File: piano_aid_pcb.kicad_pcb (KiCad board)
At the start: 2 copper layers, 44.4 x 61 mm, 35 parts, among them J1 Barrel_Jack_MountingPin, J2 796644-3, J3 DIN-5_180degree, J4 Conn_01x06_Female, J5 Micro_SD_Card_Det, J6 Conn_01x07_Female, U1 317030213, U2 6N138, U3 74AHCT1G125W5-7, U4 AZ1117-3.3

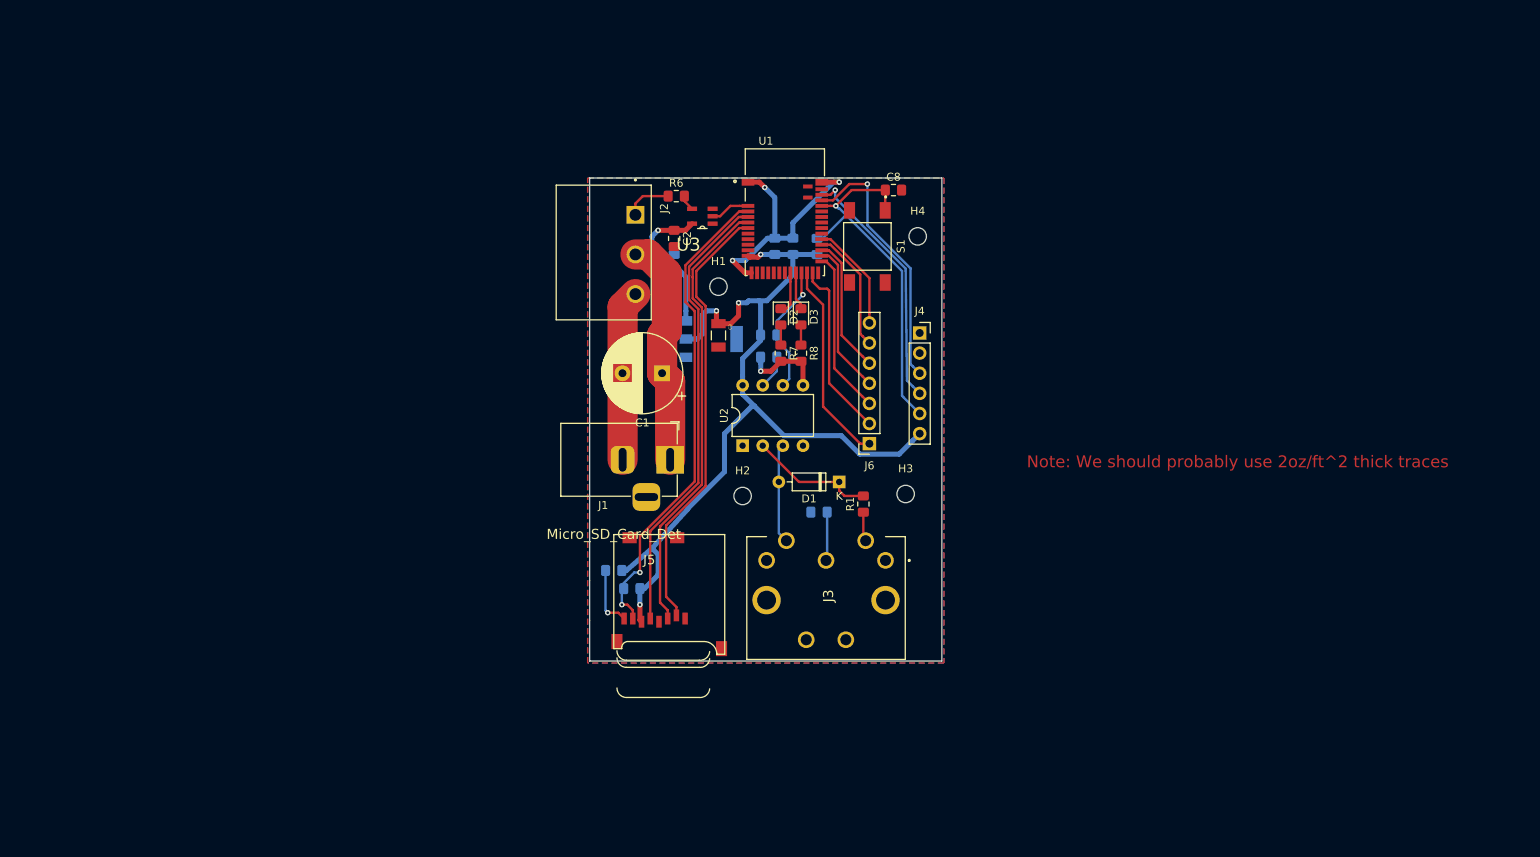
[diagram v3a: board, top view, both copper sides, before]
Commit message: Made some adjustments. Fixed silkscreen. Added team info.
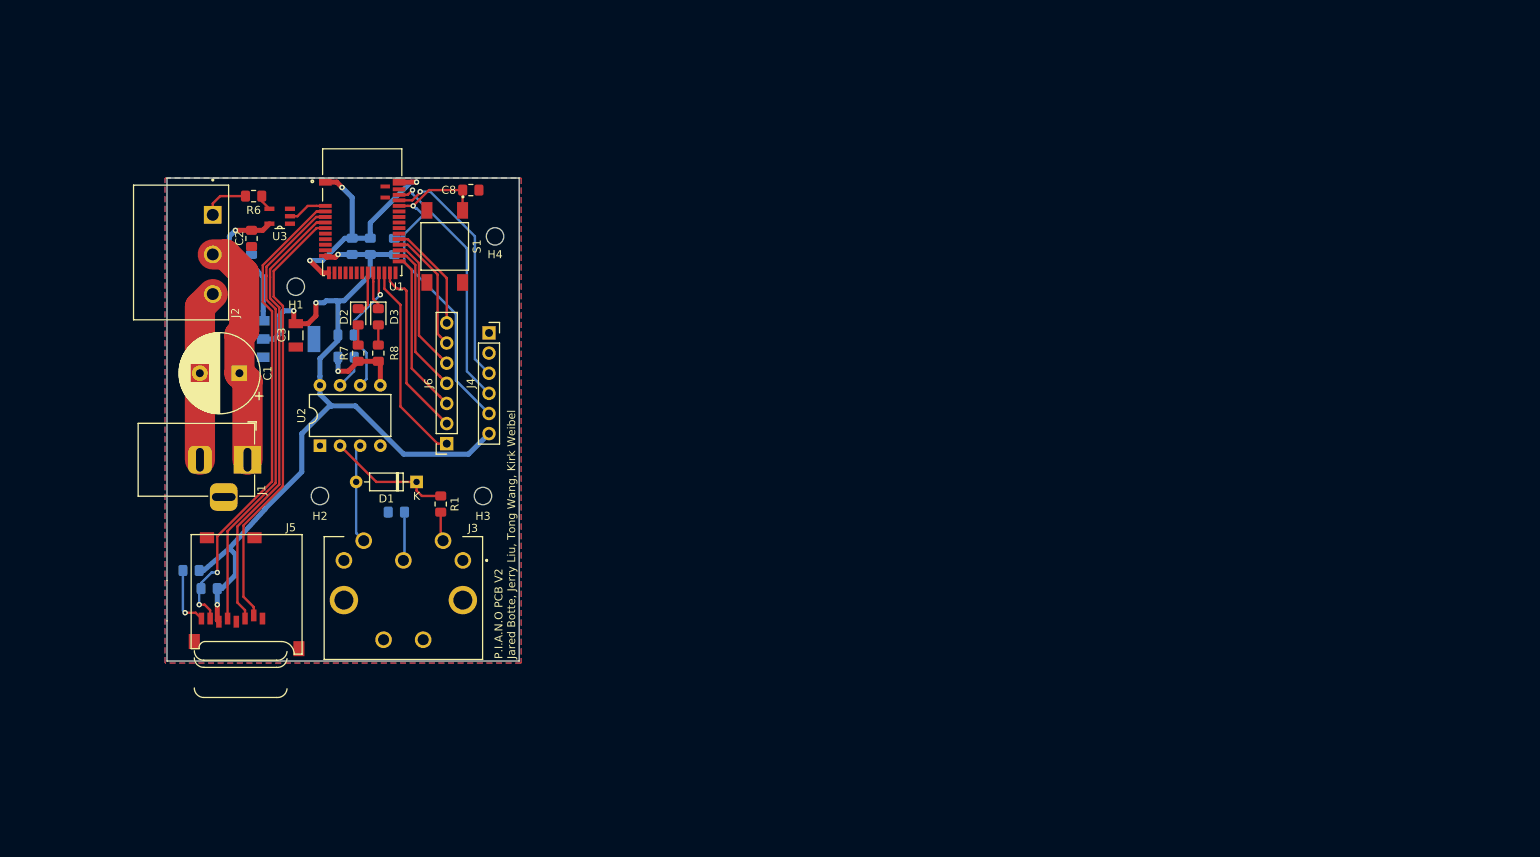
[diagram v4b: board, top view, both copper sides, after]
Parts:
- moved J4 54.4 mm to (161.3, 93.2)
- moved H3 53.3 mm to (160.5, 113.8)
- moved J5 53.3 mm to (123.7, 118.6)
- moved C3 53.3 mm to (136.9, 93.5)
- moved C5 53.3 mm to (149.6, 115.8)
- moved C6 53.3 mm to (146.3, 82.3)
- moved C7 53.3 mm to (144.0, 82.3)
- moved C8 53.3 mm to (159.0, 75.2)
- moved D1 53.3 mm to (152.1, 112.0)
- moved D2 53.3 mm to (144.8, 91.2)
- moved D3 53.3 mm to (147.3, 91.2)
- moved H1 53.3 mm to (136.9, 87.4)
- moved H2 53.3 mm to (140.0, 113.8)
- moved H4 53.3 mm to (162.1, 81.0)
- moved J1 53.3 mm to (130.8, 109.2)
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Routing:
- net SWDCLK: track 33.2 -> 30.4 mm
- net RESET: track 47.1 -> 45.4 mm
- net 3.3V: track 111.4 -> 110.4 mm
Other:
- board text added: "P.I.A.N.O PCB V2 Jared Botte Jerry Liu Tong Wang Kirk Weibel"
- board text added: "P.I.A.N.O PCB V2 Jared Botte, Jerry Liu, Tong Wang, Kirk Weibel"

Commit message: Fixed some silkscreen issues. Also fixed microsd footprint and added chip detect functionality
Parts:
- added R10: 10k, Resistor_SMD:R_0805_2012Metric_Pad1.15x1.40mm_HandSolder, B.Cu at (123.2, 116.6)
- J5: footprint adafruit:MICROSD -> microsd:MICROSD
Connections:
- U1 pad 7: Net-(U1-Pad7) -> DET
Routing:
- net DET: track 0.00 -> 51.3 mm, vias 0 -> 2
- net 3.3V: track 110.4 -> 118.0 mm
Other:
- board text added: "RESET"

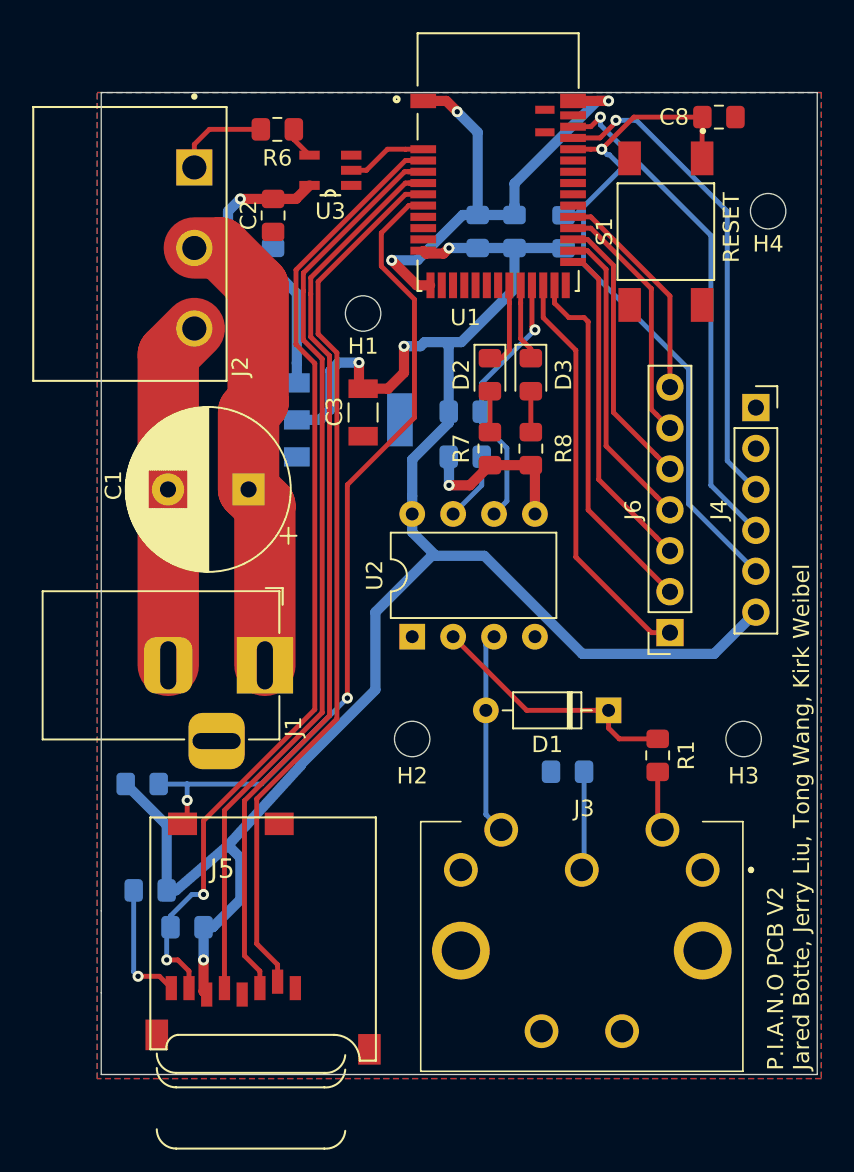
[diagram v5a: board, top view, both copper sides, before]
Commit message: Changed out barrel jack. Still needs to be connected to ground. I think there's an issue with the footprint. Also rounded the edges of the board.
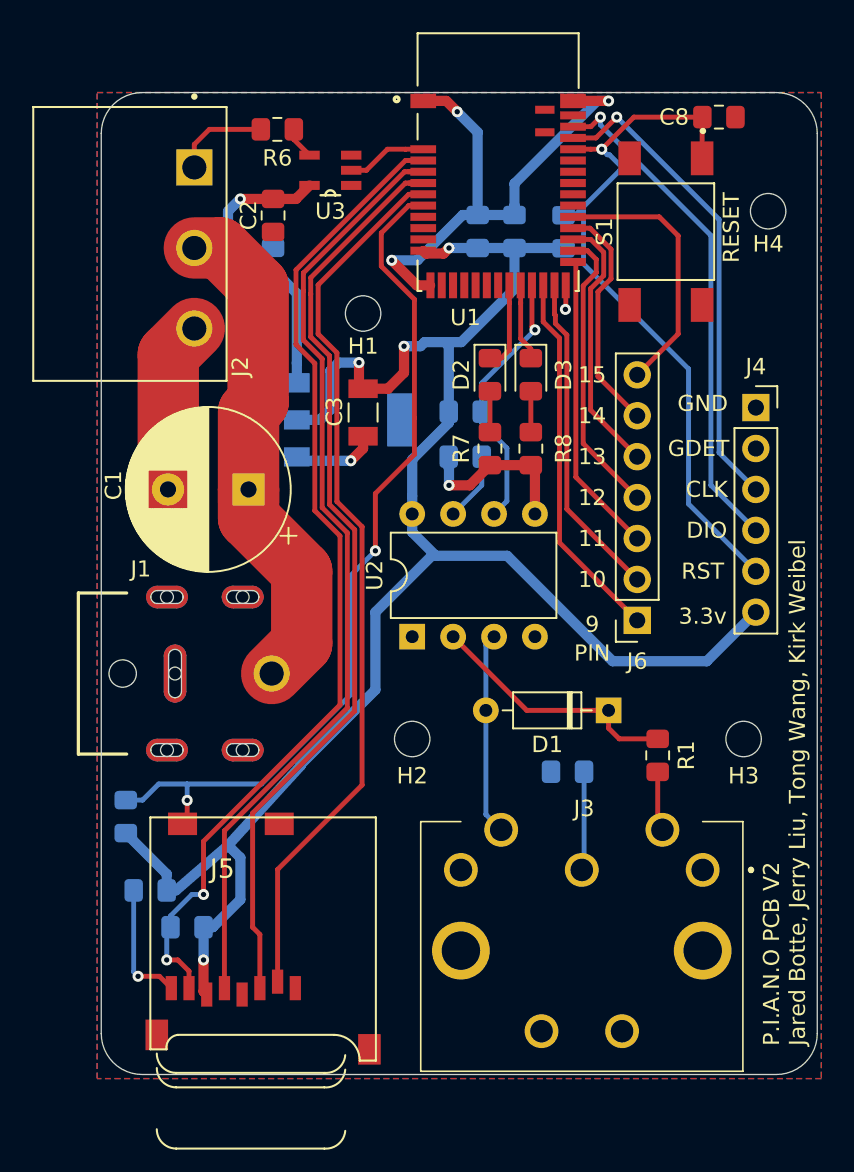
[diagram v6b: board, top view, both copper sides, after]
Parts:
- C8: value C -> 0.01µ
- J1: value Barrel_Jack_MountingPin -> PJ-082BH; footprint Connector_BarrelJack:BarrelJack_Horizontal -> PJ-082BH:CUI_PJ-082BH
- R9: value 10k -> 50k
- moved J1 5.11 mm to (125.7, 109.7)
- moved R10 2.26 mm to (122.2, 118.6), turned to 90 degrees
- moved J6 2.17 mm to (153.9, 106.4)
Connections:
- J3 pad 1: Net-(J3-Pad1) -> (no net)
- J3 pad 3: Net-(J3-Pad3) -> (no net)
- J5 pad 1: Net-(J5-Pad1) -> (no net)
- J5 pad 10: Net-(J5-Pad10) -> (no net)
- U1 pad 10: Net-(U1-Pad10) -> (no net)
- U1 pad 13: Net-(U1-Pad13) -> (no net)
- U1 pad 14: Net-(U1-Pad14) -> (no net)
- U1 pad 15: Net-(U1-Pad15) -> (no net)
- U1 pad 16: Net-(U1-Pad16) -> (no net)
- U1 pad 17: Net-(U1-Pad17) -> (no net)
- U1 pad 18: Net-(U1-Pad18) -> (no net)
- U1 pad 30: Net-(U1-Pad30) -> (no net)
- U1 pad 31: Net-(U1-Pad31) -> (no net)
- U1 pad 32: Net-(U1-Pad32) -> (no net)
- U1 pad 33: Net-(U1-Pad33) -> (no net)
- U1 pad 34: Net-(U1-Pad34) -> (no net)
- U1 pad 38: Net-(U1-Pad38) -> (no net)
- U1 pad 40: Net-(U1-Pad40) -> (no net)
- U1 pad 41: Net-(U1-Pad41) -> (no net)
- U1 pad 8: Net-(U1-Pad8) -> (no net)
- U1 pad 9: Net-(U1-Pad9) -> (no net)
- U2 pad 1: Net-(U2-Pad1) -> (no net)
- U2 pad 4: Net-(U2-Pad4) -> (no net)
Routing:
- net GND: track 65.4 -> 61.3 mm, vias 4 -> 6
- net 5V: track 50.3 -> 53.3 mm
- net P15: track 13.7 -> 16.7 mm
- net 3.3V: track 118.0 -> 115.4 mm
- net DET: track 51.3 -> 53.7 mm
- net P9: track 25.5 -> 23.2 mm
- net P10: track 22.5 -> 20.4 mm
- net P11: track 20.7 -> 18.8 mm
- net CLK: track 58.4 -> 59.7 mm
- net DAT0: track 61.9 -> 63.2 mm
- net P14: track 15.5 -> 14.6 mm
- net P12: track 19.1 -> 18.2 mm
- net CMD: track 57.5 -> 58.4 mm
- net P13: track 17.3 -> 16.5 mm
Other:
- board size 44.4 x 61 mm -> 44.5 x 61 mm
- board text added: "10"
- board text added: "11"
- board text added: "12"
- board text added: "13"
- board text added: "14"
- board text added: "15"
- board text added: "3.3v"
- board text added: "5v and 3.3v power LEDs"
- board text added: "9"
- board text added: "CLK"
- board text added: "DIO"
- board text added: "GDET"
- board text added: "GND"
- board text added: "PIN"
- board text added: "RST"

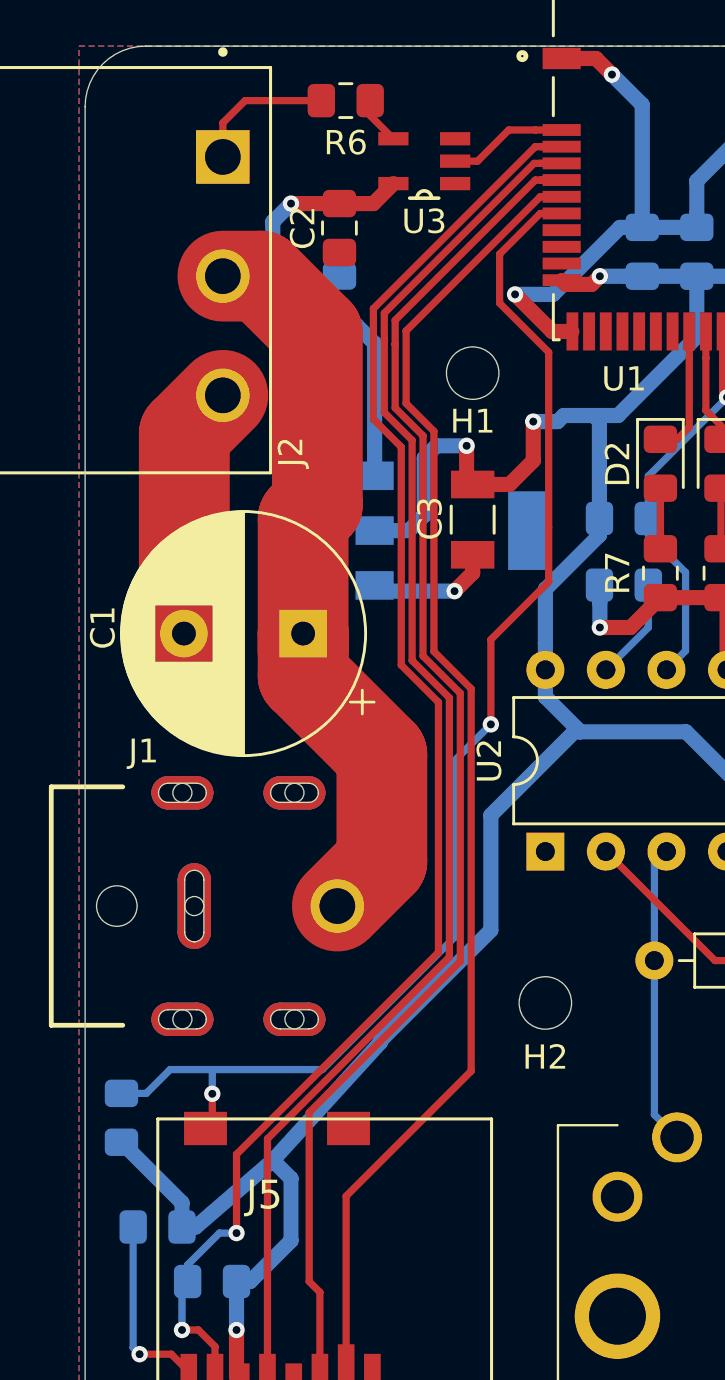
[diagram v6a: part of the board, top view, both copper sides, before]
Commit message: Created new plots, fixed barrel jack footprint, added thermal pad for power regulator, fixed fills. Instructors approve so far.
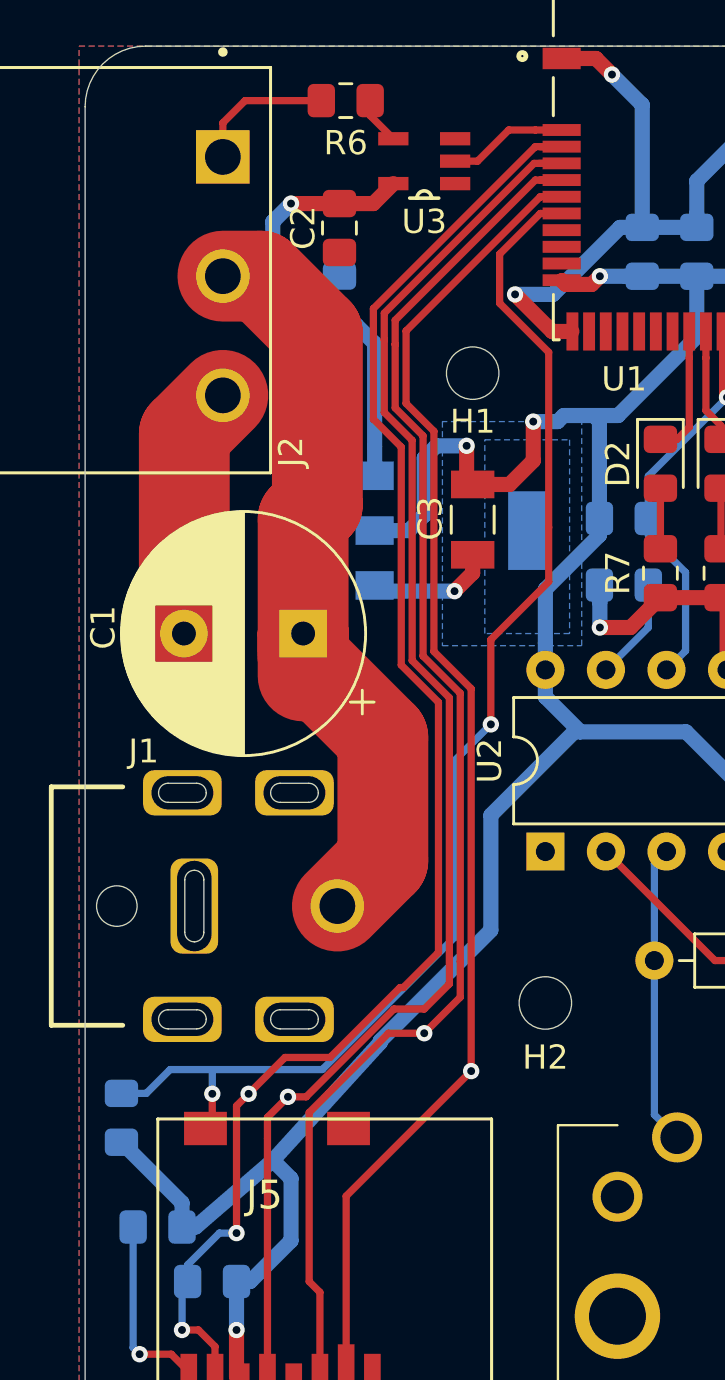
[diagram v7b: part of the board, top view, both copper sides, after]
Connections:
- J3 pad 1: (no net) -> Net-(J3-Pad1)
- J3 pad 3: (no net) -> Net-(J3-Pad3)
- J5 pad 1: (no net) -> Net-(J5-Pad1)
- J5 pad 10: (no net) -> Net-(J5-Pad10)
- U1 pad 10: (no net) -> Net-(U1-Pad10)
- U1 pad 13: (no net) -> Net-(U1-Pad13)
- U1 pad 14: (no net) -> Net-(U1-Pad14)
- U1 pad 15: (no net) -> Net-(U1-Pad15)
- U1 pad 16: (no net) -> Net-(U1-Pad16)
- U1 pad 17: (no net) -> Net-(U1-Pad17)
- U1 pad 18: (no net) -> Net-(U1-Pad18)
- U1 pad 30: (no net) -> Net-(U1-Pad30)
- U1 pad 31: (no net) -> Net-(U1-Pad31)
- U1 pad 32: (no net) -> Net-(U1-Pad32)
- U1 pad 33: (no net) -> Net-(U1-Pad33)
- U1 pad 34: (no net) -> Net-(U1-Pad34)
- U1 pad 38: (no net) -> Net-(U1-Pad38)
- U1 pad 40: (no net) -> Net-(U1-Pad40)
- U1 pad 41: (no net) -> Net-(U1-Pad41)
- U1 pad 8: (no net) -> Net-(U1-Pad8)
- U1 pad 9: (no net) -> Net-(U1-Pad9)
- U2 pad 1: (no net) -> Net-(U2-Pad1)
- U2 pad 4: (no net) -> Net-(U2-Pad4)
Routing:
- net 5V: track 53.3 -> 55.1 mm
- net CLK: track 59.7 -> 61.1 mm, vias 0 -> 1
- net DAT0: track 63.2 -> 64.4 mm, vias 2 -> 3
- net CMD: track 58.4 -> 59.2 mm, vias 0 -> 1
- net CD: vias 0 -> 1
- added copper zone on B.Cu, net 3.3V

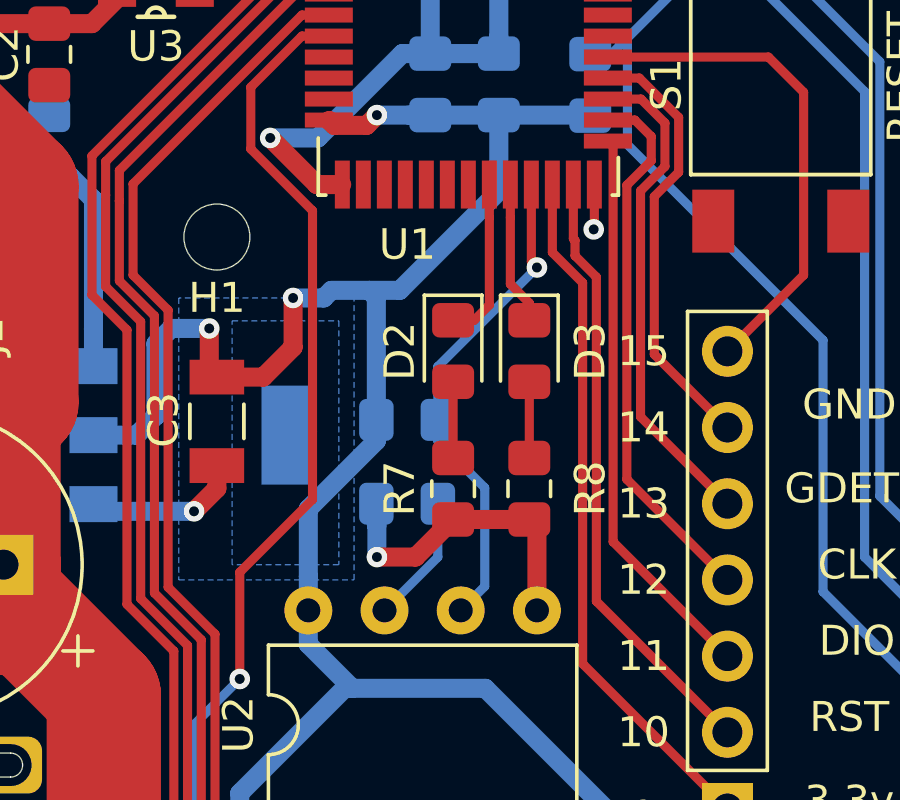
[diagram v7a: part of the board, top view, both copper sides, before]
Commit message: Fixed absolute paths, added pull up resistor.
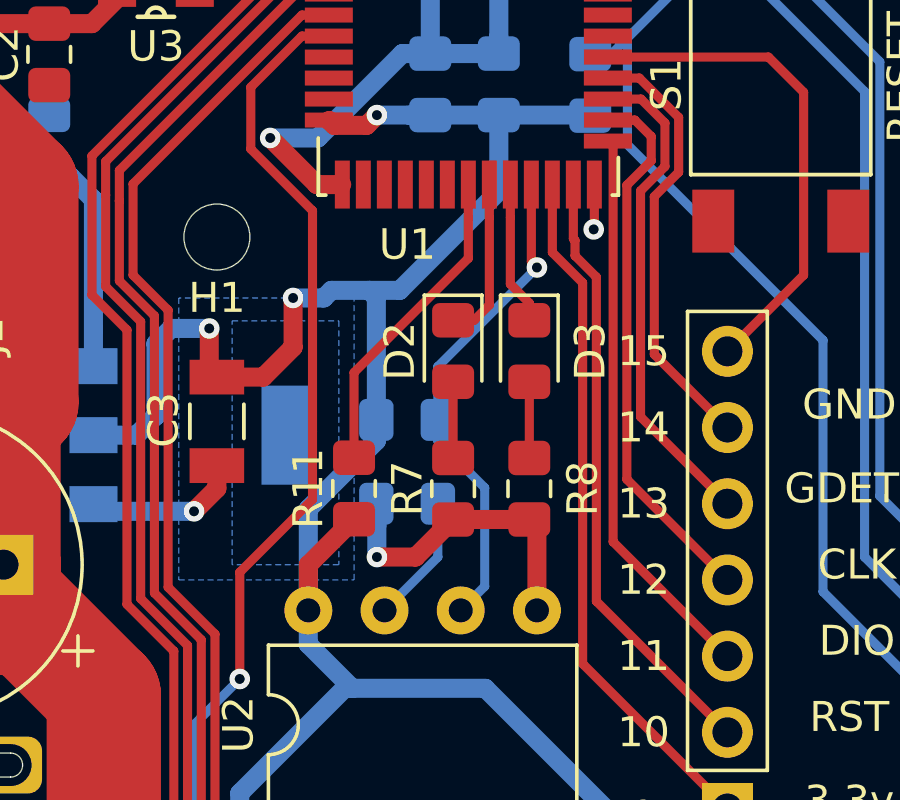
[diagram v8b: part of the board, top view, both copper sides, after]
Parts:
- added R11: 10k, Resistor_SMD:R_0805_2012Metric_Pad1.15x1.40mm_HandSolder, F.Cu at (141.5, 95.8)
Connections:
- J1 pad SHIELD: GND -> (no net)
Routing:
- net Net-(R11-Pad1): track 0.00 -> 10.7 mm
- net 3.3V: track 115.4 -> 119.0 mm
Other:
- board text removed: "5v and 3.3v power LEDs"
